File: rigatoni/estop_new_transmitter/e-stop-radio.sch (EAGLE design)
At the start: 72 parts, among them J1 E-STOP HEADER, J2 AVR_SPI_PROG_3X2PTH, J3 UX60-MB-5S8, J4 5-1814832-1, Q1 MMUN2133LT1G, U1 ATMEGA32U4-AU, U2 MCP73831T-2ACI/OT, U3 TPS62203DBVR, U4 TPS61090RSAR, U5 RFM69HCW, U6 SN74ALVC164245DGGR, X1 TSX-3225 16.0000MF18X-AC0

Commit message: First Draft Done!
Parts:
- removed J1: E-STOP HEADER, SparkFun-Connectors:CONN_11
- removed LBO: RED, microbuilder:LED0805_NOOUTLINE
- removed LED5: ORANGE, microbuilder:LED0805_NOOUTLINE
- removed R27: 1K, microbuilder:RESISTOR0805_NOOUTLINE
- removed R3: 470, microbuilder:RESISTOR0805_NOOUTLINE
- added J5: (no value), SparkFun-Connectors:CONN_15
- added R17, R18: 330, rcl:R-US_R0603
- added SW1: (no value), special:SW_DIP-1
- R12: value 0Ω -> 330
- R3\, R4, R5: value 330 -> 1k
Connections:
- net DIO_4 renamed LED_1
- net DIO_5 renamed LED_2
- net DIO_7 renamed LED_4
- removed net DIO_1: J1.3, U1.PD6(T1/ADC9/!OC4D)
- removed net DIO_2: J1.4, U1.PD7(OC4D/ADC10/T0)
- removed net DIO_3: J1.5, U1.PB4(ADC11)
- removed net DIO_6: R3\.1, U1.PC6(OC3A/!OC4A)
- removed net N$17: LBO.A, R27.1
- removed net N$19: Q1.C, R27.2
- removed net N$9: R15.2, R3.2, U2.STAT
- new net BUTTN_1: J5.14, U1.PD6(T1/ADC9/!OC4D)
- new net BUTTN_2: J5.13, U1.PD7(OC4D/ADC10/T0)
- new net BUTTN_3: J5.12, U1.PB4(ADC11)
- new net BUTTN_4: J5.11, U1.PC6(OC3A/!OC4A)
- new net DIO_7_R1: J5.6, R12.2
- new net DIO_7_R2: J5.5, R17.2
- new net DIO_7_R3: J5.4, R18.2
- new net H4: D4.A, J5.3
- new net LED_3: R3\.1
- new net LED_5: R12.1, U1.PF7(ADC7(TDI)
- new net LED_6: U1.PF6(ADC6/TDO)
- new net LED_7: Q1.C, R18.1
- new net N$15: J5.1
- net +3.3V: now also SW1.2; no longer R12.1
- net 5V_UNFUSED: now also R17.1; no longer D4.A, J1.10
- net CHARGER: no longer LED5.A
- net DIO_4_R: now also J5.10; no longer J1.6
- net DIO_5_R: now also J5.9; no longer J1.7
- net DIO_6_R: now also J5.8; no longer J1.8
- net DIO_7_R: now also J5.7; no longer J1.9
- net ENABLE: now also J5.2; no longer J1.2
- net GND: now also J5.15; no longer J1.1, J1.11, LBO.C
- net LED3: now also U1.PD4(ICP1/ADC8); no longer U1.PD5(XCK/CTS)
- net LED4: now also U1.PD1(INT1/SDA); no longer U1.PD3(INT3/TXD1)
- net N$8: now also R15.2, U2.STAT; no longer LED5.C, R3.1
- net SHIFTER_EN: now also SW1.1; no longer R12.2
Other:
- note added: "To interface header"
- moved on the sheet: C13, C14, D4, LED6, R13, R15, R22, R4, R5

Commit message: Rough PCB Design Complete
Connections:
- net BUTTN_1: now also J5.12; no longer J5.14
- net BUTTN_2: now also J5.11; no longer J5.13
- net BUTTN_3: now also J5.10; no longer J5.12
- net BUTTN_4: now also J5.9; no longer J5.11
- net DIO_4_R: now also J5.8; no longer J5.10
- net DIO_5_R: now also J5.7; no longer J5.9
- net DIO_6_R: now also J5.6; no longer J5.8
- net DIO_7_R: now also J5.5; no longer J5.7
- net DIO_7_R1: now also J5.4; no longer J5.6
- net DIO_7_R2: now also J5.3; no longer J5.5
- net DIO_7_R3: now also J5.13; no longer J5.4
- net ENABLE: now also J5.14; no longer J5.2
- net H4: now also J5.2; no longer J5.3
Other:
- moved on the sheet: J5, R12, R18, R2, R3\, R4, R5

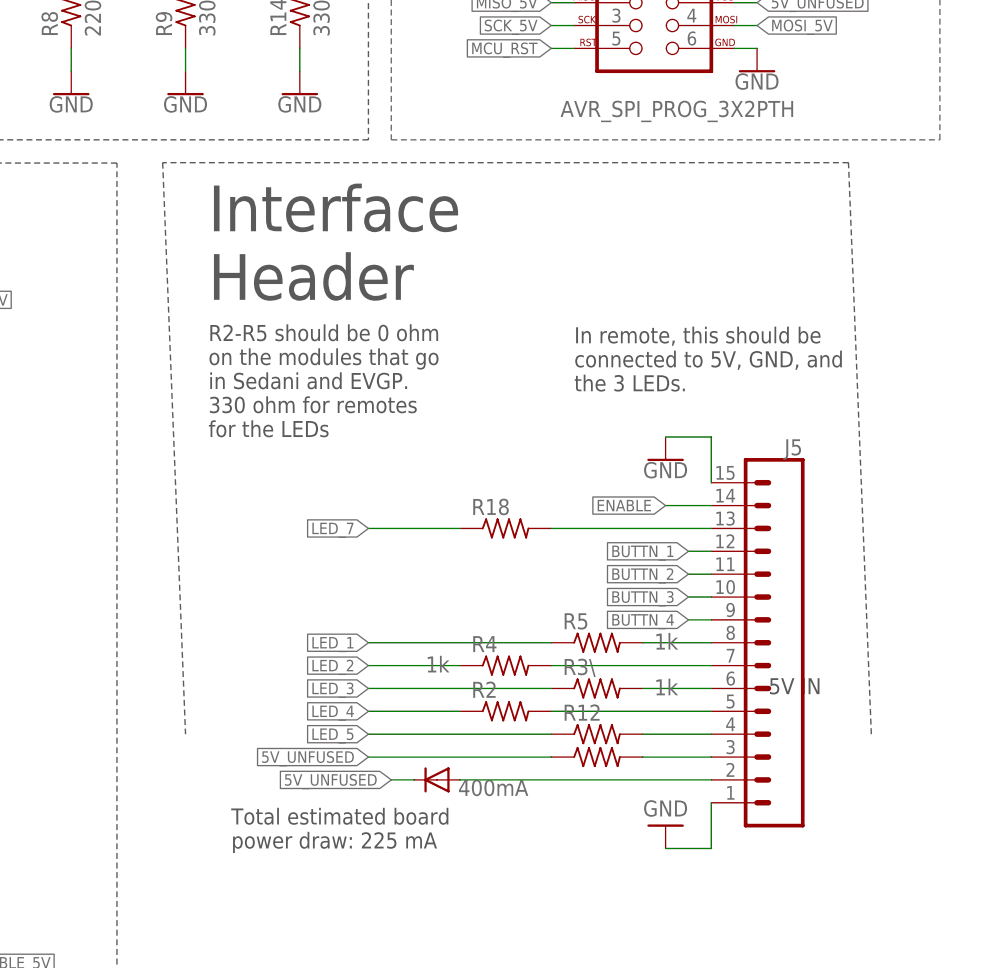
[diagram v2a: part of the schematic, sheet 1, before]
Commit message: eStopV2 Rough Draft Complete
Optimization is still needed
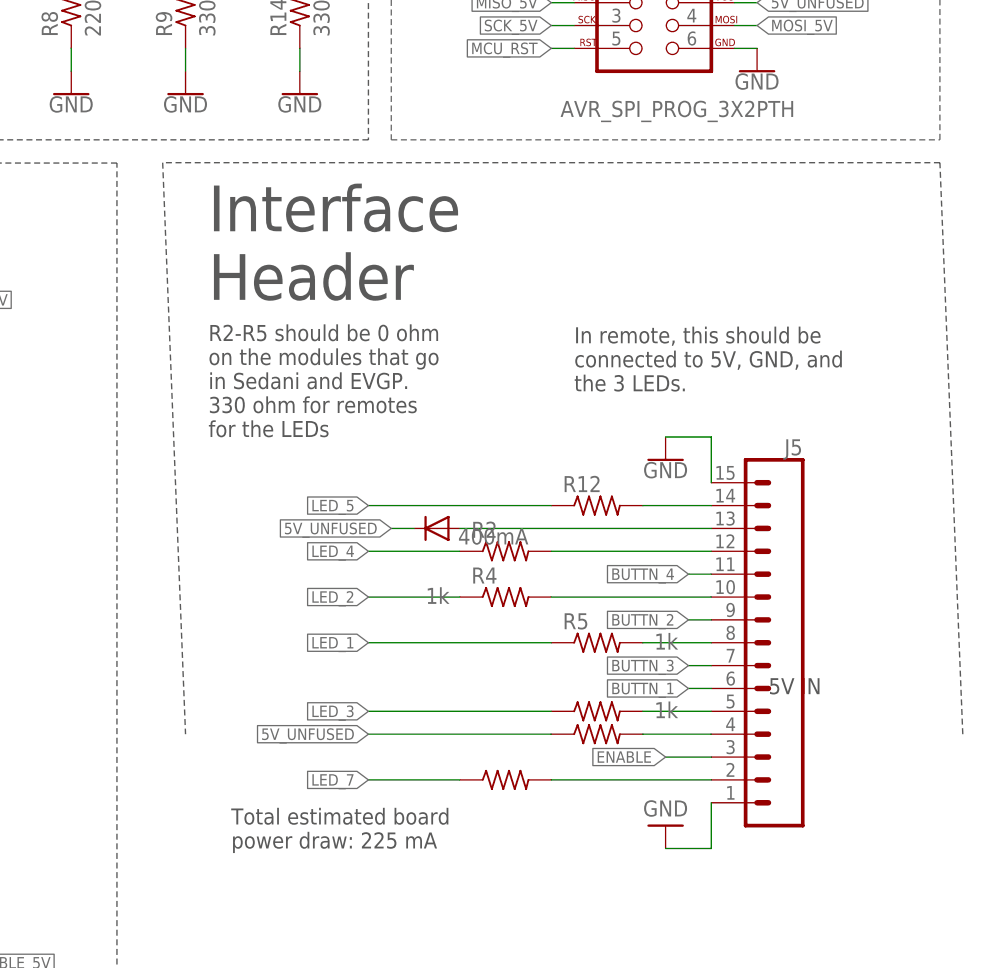
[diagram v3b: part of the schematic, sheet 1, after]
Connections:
- net BUTTN_1: now also J5.6; no longer J5.12
- net BUTTN_2: now also J5.9; no longer J5.11
- net BUTTN_3: now also J5.7; no longer J5.10
- net BUTTN_4: now also J5.11; no longer J5.9
- net DIO_5_R: now also J5.10; no longer J5.7
- net DIO_6_R: now also J5.5; no longer J5.6
- net DIO_7_R: now also J5.12; no longer J5.5
- net DIO_7_R1: now also J5.14; no longer J5.4
- net DIO_7_R2: now also J5.4; no longer J5.3
- net DIO_7_R3: now also J5.2; no longer J5.13
- net ENABLE: now also J5.3; no longer J5.14
- net H4: now also J5.13; no longer J5.2
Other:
- moved on the sheet: R12, R2, R4
